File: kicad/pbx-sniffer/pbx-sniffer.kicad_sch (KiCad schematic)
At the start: 1 part

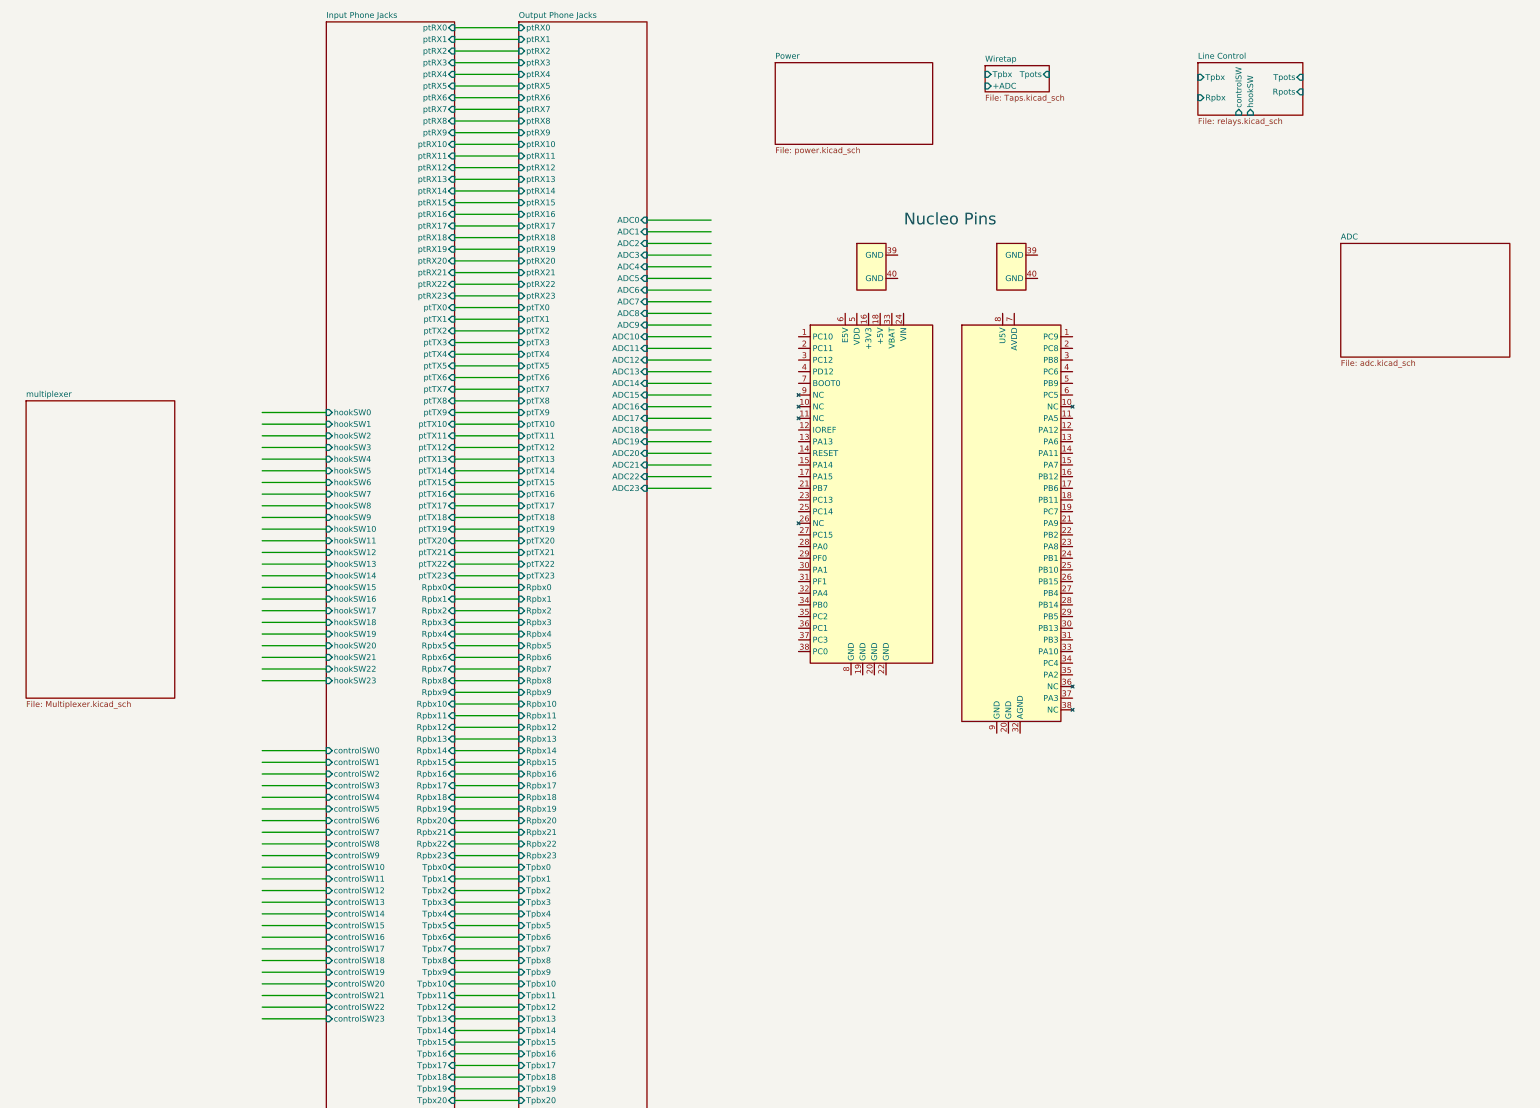
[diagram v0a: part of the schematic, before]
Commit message: wired data lines on sch
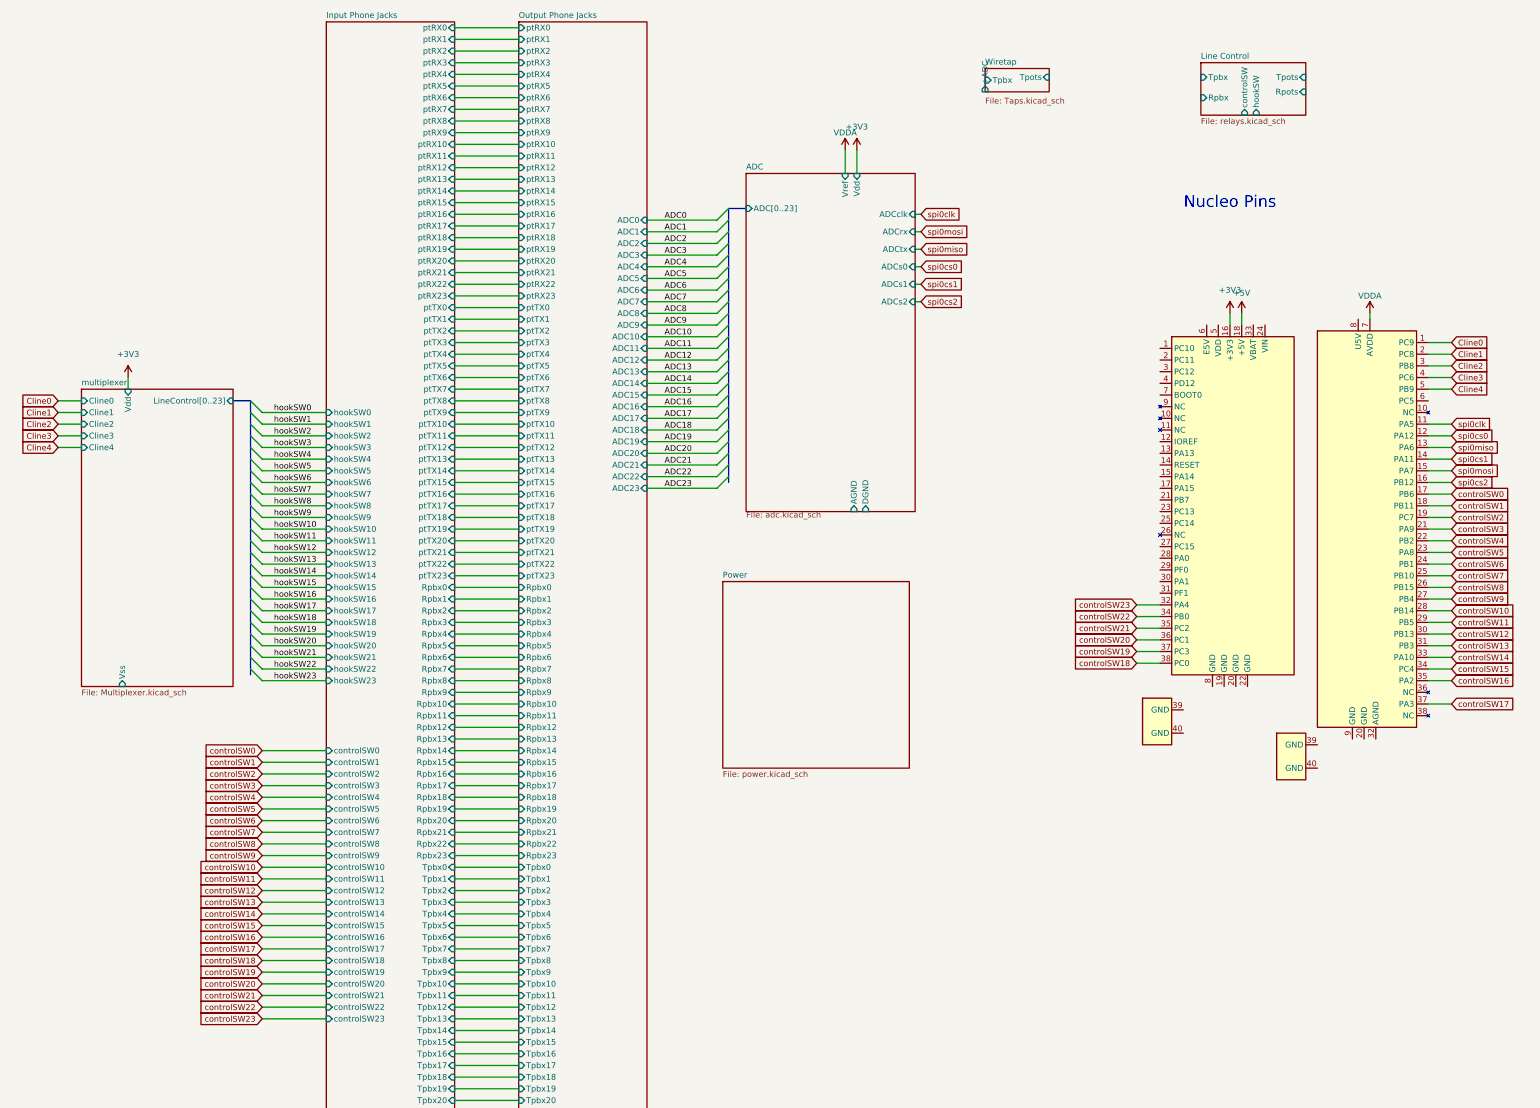
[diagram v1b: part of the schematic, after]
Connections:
- net Cline0: now reaches U1.1 (PC9)
- net spi0clk: now reaches U1.11 (PA5)
- net spi0cs0: now reaches U1.12 (PA12)
- net spi0miso: now reaches U1.13 (PA6)
- net spi0cs1: now reaches U1.14 (PA11)
- net spi0mosi: now reaches U1.15 (PA7)
- net spi0cs2: now reaches U1.16 (PB12)
- net controlSW0: now reaches U1.17 (PB6)
- net controlSW1: now reaches U1.18 (PB11)
- net controlSW2: now reaches U1.19 (PC7)
- net Cline1: now reaches U1.2 (PC8)
- net controlSW3: now reaches U1.21 (PA9)
- net controlSW4: now reaches U1.22 (PB2)
- net controlSW5: now reaches U1.23 (PA8)
- net controlSW6: now reaches U1.24 (PB1)
- net controlSW7: now reaches U1.25 (PB10)
- net controlSW8: now reaches U1.26 (PB15)
- net controlSW9: now reaches U1.27 (PB4)
- net controlSW10: now reaches U1.28 (PB14)
- net controlSW11: now reaches U1.29 (PB5)
- net Cline2: now reaches U1.3 (PB8)
- net controlSW12: now reaches U1.30 (PB13)
- net controlSW13: now reaches U1.31 (PB3)
- net controlSW14: now reaches U1.33 (PA10)
- net controlSW15: now reaches U1.34 (PC4)
- net controlSW16: now reaches U1.35 (PA2)
- net controlSW17: now reaches U1.37 (PA3)
- net Cline3: now reaches U1.4 (PC6)
- net Cline4: now reaches U1.5 (PB9)
- net VDDA: now reaches U1.7 (AVDD)
- net +3V3: now reaches U1.16 (+3V3)
- net +5V: now reaches U1.18 (+5V)
- net controlSW23: now reaches U1.32 (PA4)
- net controlSW22: now reaches U1.34 (PB0)
- net controlSW21: now reaches U1.35 (PC2)
- net controlSW20: now reaches U1.36 (PC1)
- net controlSW19: now reaches U1.37 (PC3)
- net controlSW18: now reaches U1.38 (PC0)
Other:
- sheet ADC ports: added ADC[0..23], ADCclk, ADCrx, ADCs0, ADCs1, ADCs2, ADCtx, AGND, DGND, Vdd, Vref; removed none
- sheet multiplexer ports: added Cline0, Cline1, Cline2, Cline3, Cline4, LineControl[0..23], Vdd, Vss; removed none

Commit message: clean up & organize schematic
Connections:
- net GND: now reaches U1.20 (GND)
- net GND: now also U1.19 (GND), U1.20 (GND), U1.22 (GND), U1.32 (AGND), U1.39 (GND), U1.39 (GND), U1.40 (GND), U1.40 (GND), U1.8 (GND), U1.9 (GND)
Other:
- note added: "Telephony Building Blocks"
- note added: "Telephony IO & Sniffing"
- note added: "WIP"

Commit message: commenced placement on pcb
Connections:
- net +3V3: now also U1.33 (VBAT)
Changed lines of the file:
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@@
 	(wire
 		(pts
+			(xy 313.69 76.2) (xy 313.69 78.74)
+		)
+		(stroke
+			(width 0)
+			(type default)
+		)
+	)
+	(wire
+		(pts
 			(xy 351.79 161.29) (xy 356.87 161.29)
 		)
@@
 	(wire
 		(pts
-			(xy 311.15 76.2) (xy 311.15 78.74)
+			(xy 311.15 73.66) (xy 311.15 78.74)
 		)
 		(stroke
@@
 		(on_board yes)
 		(dnp no)
-		(property "Reference" "#PWR0240"
+		(property "Reference" "#PWR05"
 			(at 308.61 80.01 0)
 			(effects
@@
 			(project ""
 				(path "/4a5b9b8a-323a-4796-bf73-ccba532d2e31"
-					(reference "#PWR0240")
+					(reference "#PWR05")
 					(unit 1)
 				)
@@
 		(dnp no)
 		(fields_autoplaced yes)
-		(property "Reference" "#PWR0243"
+		(property "Reference" "#PWR06"
 			(at 308.61 167.64 0)
 			(effects
@@
 			(project ""
 				(path "/4a5b9b8a-323a-4796-bf73-ccba532d2e31"
-					(reference "#PWR0243")
+					(reference "#PWR06")
 					(unit 1)
 				)
@@
 		(dnp no)
 		(fields_autoplaced yes)
-		(property "Reference" "#PWR0237"
+		(property "Reference" "#PWR011"
 			(at 339.09 80.01 0)
 			(effects
@@
 			(project "pbx-sniffer"
 				(path "/4a5b9b8a-323a-4796-bf73-ccba532d2e31"
-					(reference "#PWR0237")
+					(reference "#PWR011")
 					(unit 1)
 				)
@@
 		(dnp no)
 		(fields_autoplaced yes)
-		(property "Reference" "#PWR0238"
+		(property "Reference" "#PWR02"
 			(at 228.6 57.15 0)
 			(effects
@@
 			(project "pbx-sniffer"
 				(path "/4a5b9b8a-323a-4796-bf73-ccba532d2e31"
-					(reference "#PWR0238")
+					(reference "#PWR02")
+					(unit 1)
+				)
+			)
+		)
+	)
+	(symbol
+		(lib_id "power:+3V3")
+		(at 313.69 76.2 0)
+		(unit 1)
+		(exclude_from_sim no)
+		(in_bom yes)
+		(on_board yes)
+		(dnp no)
+		(property "Reference" "#PWR08"
+			(at 313.69 80.01 0)
+			(effects
+				(font
+					(size 1.27 1.27)
+				)
+				(hide yes)
+			)
+		)
+		(property "Value" "+3V3"
+			(at 309.88 74.93 0)
+			(effects
+				(font
+					(size 1.27 1.27)
+				)
+			)
+		)
+		(property "Footprint" ""
+			(at 313.69 76.2 0)
+			(effects
+				(font
+					(size 1.27 1.27)
+				)
+				(hide yes)
+			)
+		)
+		(property "Datasheet" ""
+			(at 313.69 76.2 0)
+			(effects
+				(font
+					(size 1.27 1.27)
+				)
+				(hide yes)
+			)
+		)
+		(property "Description" "Power symbol creates a global label with name \"+3V3\""
+			(at 313.69 76.2 0)
+			(effects
+				(font
+					(size 1.27 1.27)
+				)
+				(hide yes)
+			)
+		)
+		(pin "1"
+		)
+		(instances
+			(project "pbx-sniffer"
+				(path "/4a5b9b8a-323a-4796-bf73-ccba532d2e31"
+					(reference "#PWR08")
 					(unit 1)
 				)
@@
 		(on_board yes)
 		(dnp no)
-		(property "Reference" "#PWR0246"
+		(property "Reference" "#PWR09"
 			(at 332.74 74.93 0)
 			(effects
@@
 			(project "pbx-sniffer"
 				(path "/4a5b9b8a-323a-4796-bf73-ccba532d2e31"
-					(reference "#PWR0246")
+					(reference "#PWR09")
 					(unit 1)
 				)
@@
 		(on_board yes)
 		(dnp no)
-		(property "Reference" "#PWR0241"
+		(property "Reference" "#PWR03"
 			(at 231.14 57.15 0)
 			(effects
@@
 			(project "pbx-sniffer"
 				(path "/4a5b9b8a-323a-4796-bf73-ccba532d2e31"
-					(reference "#PWR0241")
+					(reference "#PWR03")
 					(unit 1)
 				)
@@
 	(symbol
 		(lib_id "power:+5V")
-		(at 311.15 76.2 0)
+		(at 311.15 73.66 0)
 		(unit 1)
 		(exclude_from_sim no)
@@
 		(on_board yes)
 		(dnp no)
-		(property "Reference" "#PWR0239"
-			(at 311.15 80.01 0)
+		(property "Reference" "#PWR07"
+			(at 311.15 77.47 0)
 			(effects
 				(font
@@
 		)
 		(property "Value" "+5V"
-			(at 313.69 74.93 0)
+			(at 313.69 72.39 0)
 			(effects
 				(font
@@
 		)
 		(property "Footprint" ""
-			(at 311.15 76.2 0)
+			(at 311.15 73.66 0)
 			(effects
 				(font
@@
 		)
 		(property "Datasheet" ""
-			(at 311.15 76.2 0)
+			(at 311.15 73.66 0)
 			(effects
 				(font
@@
 		)
 		(property "Description" "Power symbol creates a global label with name \"+5V\""
-			(at 311.15 76.2 0)
+			(at 311.15 73.66 0)
 			(effects
 				(font
@@
 			(project "pbx-sniffer"
 				(path "/4a5b9b8a-323a-4796-bf73-ccba532d2e31"
-					(reference "#PWR0239")
+					(reference "#PWR07")
 					(unit 1)
 				)
@@
 		(dnp no)
 		(fields_autoplaced yes)
-		(property "Reference" "#PWR0242"
+		(property "Reference" "#PWR01"
 			(at 72.39 106.68 0)
 			(effects
@@
 			(project "pbx-sniffer"
 				(path "/4a5b9b8a-323a-4796-bf73-ccba532d2e31"
-					(reference "#PWR0242")
+					(reference "#PWR01")
 					(unit 1)
 				)
@@
 		(dnp no)
 		(fields_autoplaced yes)
-		(property "Reference" "#PWR0244"
+		(property "Reference" "#PWR010"
 			(at 337.82 179.07 0)
 			(effects
@@
 			(project "pbx-sniffer"
 				(path "/4a5b9b8a-323a-4796-bf73-ccba532d2e31"
-					(reference "#PWR0244")
+					(reference "#PWR010")
 					(unit 1)
 				)
@@
 		(on_board yes)
 		(dnp no)
-		(property "Reference" "#PWR0245"
+		(property "Reference" "#PWR04"
 			(at 300.99 74.93 0)
 			(effects
@@
 			(project "pbx-sniffer"
 				(path "/4a5b9b8a-323a-4796-bf73-ccba532d2e31"
-					(reference "#PWR0245")
+					(reference "#PWR04")
 					(unit 1)
 				)

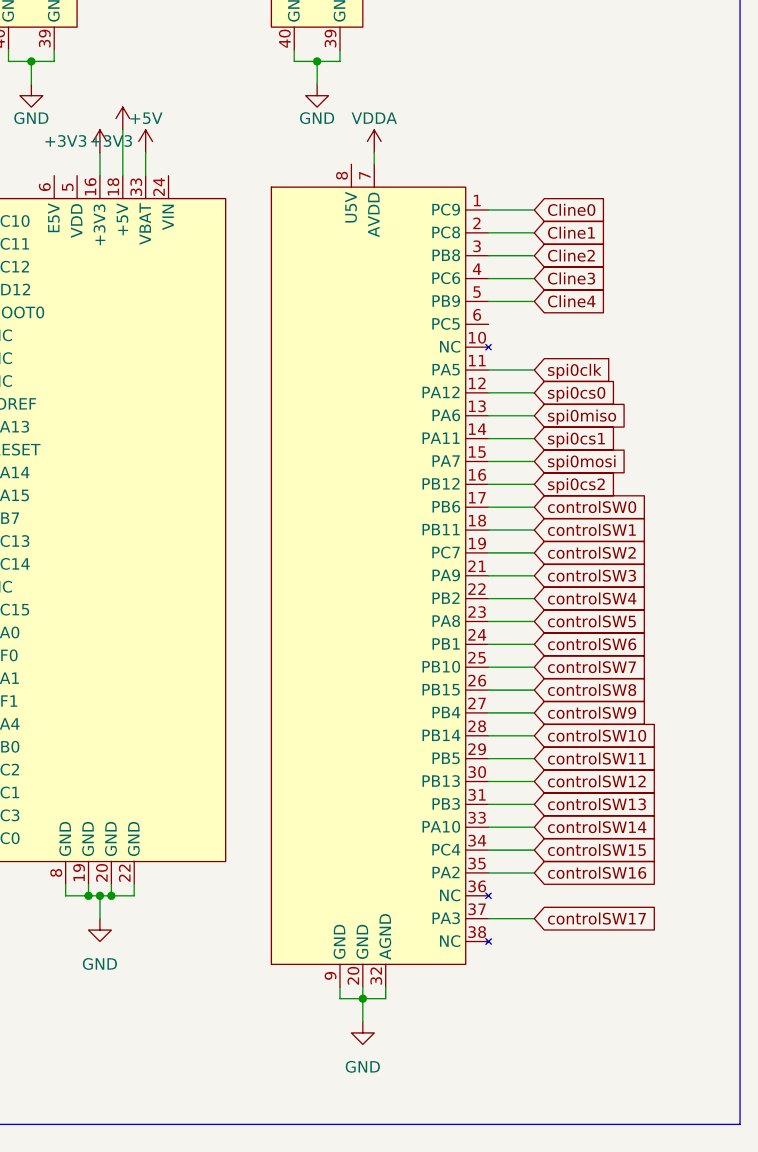
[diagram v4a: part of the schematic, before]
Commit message: fix nucleo footprint and update pin numbers
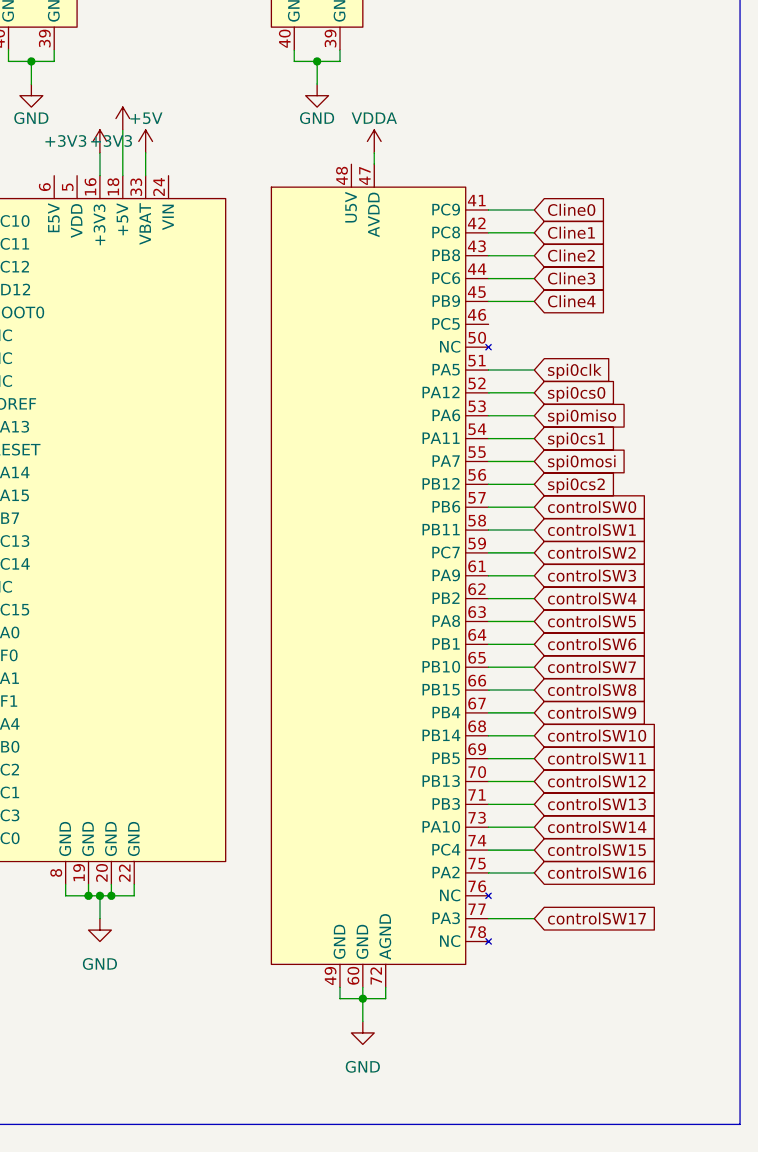
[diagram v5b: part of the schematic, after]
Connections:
- net Cline0: now also U1.41 (PC9); no longer U1.1 (PC9)
- net Cline1: now also U1.42 (PC8); no longer U1.2 (PC8)
- net Cline2: now also U1.43 (PB8); no longer U1.3 (PB8)
- net Cline3: now also U1.44 (PC6); no longer U1.4 (PC6)
- net Cline4: now also U1.45 (PB9); no longer U1.5 (PB9)
- net GND: now also U1.49 (GND), U1.60 (GND), U1.72 (AGND); no longer U1.20 (GND), U1.32 (AGND), U1.9 (GND)
- net VDDA: now also U1.47 (AVDD); no longer U1.7 (AVDD)
- net controlSW0: now also U1.57 (PB6); no longer U1.17 (PB6)
- net controlSW1: now also U1.58 (PB11); no longer U1.18 (PB11)
- net controlSW10: now also U1.68 (PB14); no longer U1.28 (PB14)
- net controlSW11: now also U1.69 (PB5); no longer U1.29 (PB5)
- net controlSW12: now also U1.70 (PB13); no longer U1.30 (PB13)
- net controlSW13: now also U1.71 (PB3); no longer U1.31 (PB3)
- net controlSW14: now also U1.73 (PA10); no longer U1.33 (PA10)
- net controlSW15: now also U1.74 (PC4); no longer U1.34 (PC4)
- net controlSW16: now also U1.75 (PA2); no longer U1.35 (PA2)
- net controlSW17: now also U1.77 (PA3); no longer U1.37 (PA3)
- net controlSW2: now also U1.59 (PC7); no longer U1.19 (PC7)
- net controlSW3: now also U1.61 (PA9); no longer U1.21 (PA9)
- net controlSW4: now also U1.62 (PB2); no longer U1.22 (PB2)
- net controlSW5: now also U1.63 (PA8); no longer U1.23 (PA8)
- net controlSW6: now also U1.64 (PB1); no longer U1.24 (PB1)
- net controlSW7: now also U1.65 (PB10); no longer U1.25 (PB10)
- net controlSW8: now also U1.66 (PB15); no longer U1.26 (PB15)
- net controlSW9: now also U1.67 (PB4); no longer U1.27 (PB4)
- net spi0clk: now also U1.51 (PA5); no longer U1.11 (PA5)
- net spi0cs0: now also U1.52 (PA12); no longer U1.12 (PA12)
- net spi0cs1: now also U1.54 (PA11); no longer U1.14 (PA11)
- net spi0cs2: now also U1.56 (PB12); no longer U1.16 (PB12)
- net spi0miso: now also U1.53 (PA6); no longer U1.13 (PA6)
- net spi0mosi: now also U1.55 (PA7); no longer U1.15 (PA7)
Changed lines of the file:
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@@
 	)
 	(symbol
+		(lib_name "STM32NucleoF303RE_1")
 		(lib_id "Phones:STM32NucleoF303RE")
 		(at 327.66 80.01 0)
@@
 		(pin "33"
 		)
-		(pin "20"
+		(pin "70"
 		)
 		(pin "40"
@@
 		(pin "31"
 		)
-		(pin "22"
+		(pin "71"
 		)
 		(pin "21"
 		)
-		(pin "10"
+		(pin "73"
 		)
 		(pin "25"
@@
 		(pin "17"
 		)
-		(pin "30"
+		(pin "74"
 		)
 		(pin "36"
 		)
-		(pin "17"
+		(pin "75"
 		)
 		(pin "39"
@@
 		(pin "38"
 		)
-		(pin "35"
-		)
-		(pin "33"
+		(pin "76"
+		)
+		(pin "53"
 		)
 		(pin "8"
 		)
-		(pin "31"
+		(pin "54"
 		)
 		(pin "34"
@@
 		(pin "24"
 		)
-		(pin "29"
+		(pin "55"
 		)
 		(pin "40"
 		)
-		(pin "38"
+		(pin "56"
 		)
 		(pin "15"
@@
 		(pin "28"
 		)
-		(pin "21"
-		)
-		(pin "8"
-		)
-		(pin "28"
+		(pin "57"
+		)
+		(pin "58"
+		)
+		(pin "44"
 		)
 		(pin "14"
 		)
-		(pin "15"
+		(pin "45"
 		)
 		(pin "12"
@@
 		(pin "6"
 		)
-		(pin "1"
-		)
-		(pin "2"
-		)
-		(pin "3"
-		)
-		(pin "34"
+		(pin "46"
+		)
+		(pin "50"
+		)
+		(pin "51"
+		)
+		(pin "52"
 		)
 		(pin "4"
 		)
-		(pin "7"
-		)
-		(pin "12"
-		)
-		(pin "9"
-		)
-		(pin "13"
-		)
-		(pin "36"
-		)
-		(pin "6"
-		)
-		(pin "14"
+		(pin "49"
+		)
+		(pin "48"
+		)
+		(pin "59"
+		)
+		(pin "61"
+		)
+		(pin "62"
+		)
+		(pin "63"
+		)
+		(pin "64"
 		)
 		(pin "5"
 		)
-		(pin "5"
-		)
-		(pin "4"
-		)
-		(pin "16"
-		)
-		(pin "23"
-		)
-		(pin "19"
-		)
-		(pin "11"
-		)
-		(pin "18"
-		)
-		(pin "37"
-		)
-		(pin "32"
-		)
-		(pin "27"
-		)
-		(pin "26"
-		)
-		(pin "24"
-		)
-		(pin "25"
+		(pin "65"
+		)
+		(pin "60"
+		)
+		(pin "47"
+		)
+		(pin "72"
+		)
+		(pin "41"
+		)
+		(pin "42"
+		)
+		(pin "43"
+		)
+		(pin "77"
+		)
+		(pin "78"
+		)
+		(pin "66"
+		)
+		(pin "67"
+		)
+		(pin "68"
+		)
+		(pin "69"
 		)
 		(instances
